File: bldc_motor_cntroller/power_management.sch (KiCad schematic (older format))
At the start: 29 parts, among them J8 XT60, J9 XT60, Q1 CSD18540Q5B, Q2 CSD18540Q5B, U2 TLV75733PDBV, U3 LM5109BSD

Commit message: added missing footprints.
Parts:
- R15, R18: footprint Capacitor_SMD:C_0402_1005Metric -> Resistor_SMD:R_0402_1005Metric
- R16, R17, R19: footprint (none) -> Resistor_SMD:R_0402_1005Metric
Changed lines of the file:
@@
 F 0 "R15" V 4900 5200 50  0000 C CNN
 F 1 "2R2" V 4800 5200 50  0000 C CNN
-F 2 "Capacitor_SMD:C_0402_1005Metric" V 4730 5200 50  0001 C CNN
+F 2 "Resistor_SMD:R_0402_1005Metric" V 4730 5200 50  0001 C CNN
 F 3 "~" H 4800 5200 50  0001 C CNN
 	1    4800 5200
@@
 F 0 "R18" V 4900 5950 50  0000 C CNN
 F 1 "2R2" V 4800 5950 50  0000 C CNN
-F 2 "Capacitor_SMD:C_0402_1005Metric" V 4730 5950 50  0001 C CNN
+F 2 "Resistor_SMD:R_0402_1005Metric" V 4730 5950 50  0001 C CNN
 F 3 "~" H 4800 5950 50  0001 C CNN
 	1    4800 5950
@@
 F 0 "R19" H 3280 6854 50  0000 R CNN
 F 1 "3.3k" H 3280 6945 50  0000 R CNN
-F 2 "" V 3280 6900 50  0001 C CNN
+F 2 "Resistor_SMD:R_0402_1005Metric" V 3280 6900 50  0001 C CNN
 F 3 "~" H 3350 6900 50  0001 C CNN
 	1    3350 6900
@@
 F 0 "R17" H 2430 5904 50  0000 R CNN
 F 1 "3.3k" H 2430 5995 50  0000 R CNN
-F 2 "" V 2430 5950 50  0001 C CNN
+F 2 "Resistor_SMD:R_0402_1005Metric" V 2430 5950 50  0001 C CNN
 F 3 "~" H 2500 5950 50  0001 C CNN
 	1    2500 5950
@@
 F 0 "R16" H 2080 5904 50  0000 R CNN
 F 1 "3.3k" H 2080 5995 50  0000 R CNN
-F 2 "" V 2080 5950 50  0001 C CNN
+F 2 "Resistor_SMD:R_0402_1005Metric" V 2080 5950 50  0001 C CNN
 F 3 "~" H 2150 5950 50  0001 C CNN
 	1    2150 5950

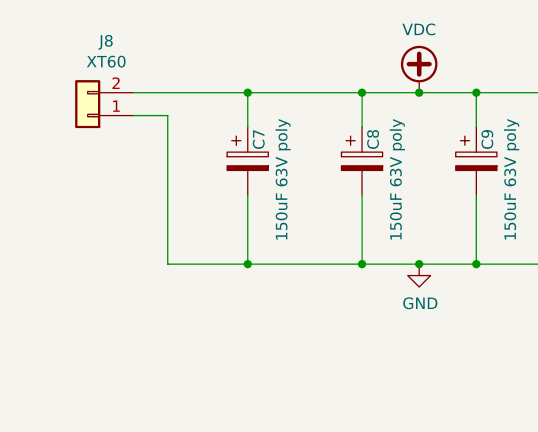
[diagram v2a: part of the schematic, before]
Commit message: pcb routing cont. swapped 2 motor output pins for better routing.
Signed-off-by: azmat bilal <azmat.bilal@outlook.com>
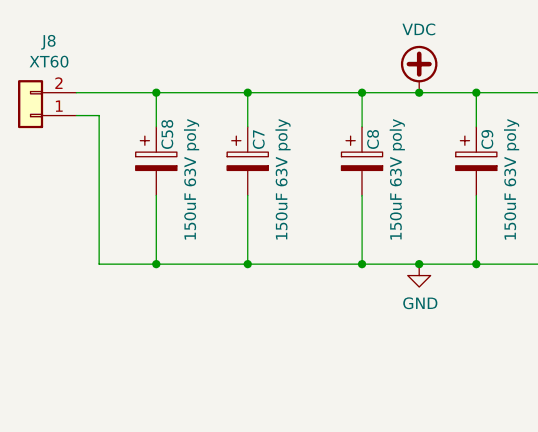
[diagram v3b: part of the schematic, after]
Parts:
- added C58: 150uF 63V poly, Capacitor_SMD:CP_Elec_10x14.3, symbol Device:CP
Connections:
- net GND: now also C58.2
- net VDC: now also C58.1
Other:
- moved on the sheet: J8
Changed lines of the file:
@@
 L Connector_Generic:Conn_01x02 J8
 U 1 1 5E3F134B
-P 1550 1750
-F 0 "J8" H 1468 1425 50  0000 C CNN
-F 1 "XT60" H 1468 1516 50  0000 C CNN
-F 2 "Connector_AMASS:AMASS_XT60-M_1x02_P7.20mm_Vertical" H 1550 1750 50  0001 C CNN
-F 3 "~" H 1550 1750 50  0001 C CNN
-	1    1550 1750
+P 1300 1750
+F 0 "J8" H 1218 1425 50  0000 C CNN
+F 1 "XT60" H 1218 1516 50  0000 C CNN
+F 2 "Connector_AMASS:AMASS_XT60-M_1x02_P7.20mm_Vertical" H 1300 1750 50  0001 C CNN
+F 3 "~" H 1300 1750 50  0001 C CNN
+	1    1300 1750
 	-1   0    0    1
 $EndComp
-Wire Wire Line
-	1750 1650 2250 1650
 Connection ~ 2250 1650
-Wire Wire Line
-	1750 1750 1900 1750
-Wire Wire Line
-	1900 1750 1900 2400
-Wire Wire Line
-	1900 2400 2250 2400
 Connection ~ 2250 2400
 $Comp
@@
 	0    1    1    0
 $EndComp
+$Comp
+L Device:CP C58
+U 1 1 5E4177F9
+P 1850 1950
+F 0 "C58" V 1900 2000 50  0000 L CNN
+F 1 "150uF 63V poly" V 2000 1600 50  0000 L CNN
+F 2 "Capacitor_SMD:CP_Elec_10x14.3" H 1888 1800 50  0001 C CNN
+F 3 "~" H 1850 1950 50  0001 C CNN
+F 4 "EEH-ZS1J151P" H 1850 1950 50  0001 C CNN "MPN"
+	1    1850 1950
+	1    0    0    -1
+$EndComp
+Wire Wire Line
+	1850 2100 1850 2400
+Wire Wire Line
+	1850 2400 2250 2400
+Wire Wire Line
+	1850 1800 1850 1650
+Connection ~ 1850 1650
+Wire Wire Line
+	1850 1650 2250 1650
+Wire Wire Line
+	1500 1650 1850 1650
+Wire Wire Line
+	1500 1750 1600 1750
+Wire Wire Line
+	1600 1750 1600 2400
+Wire Wire Line
+	1600 2400 1850 2400
+Connection ~ 1850 2400
 $EndSCHEMATC

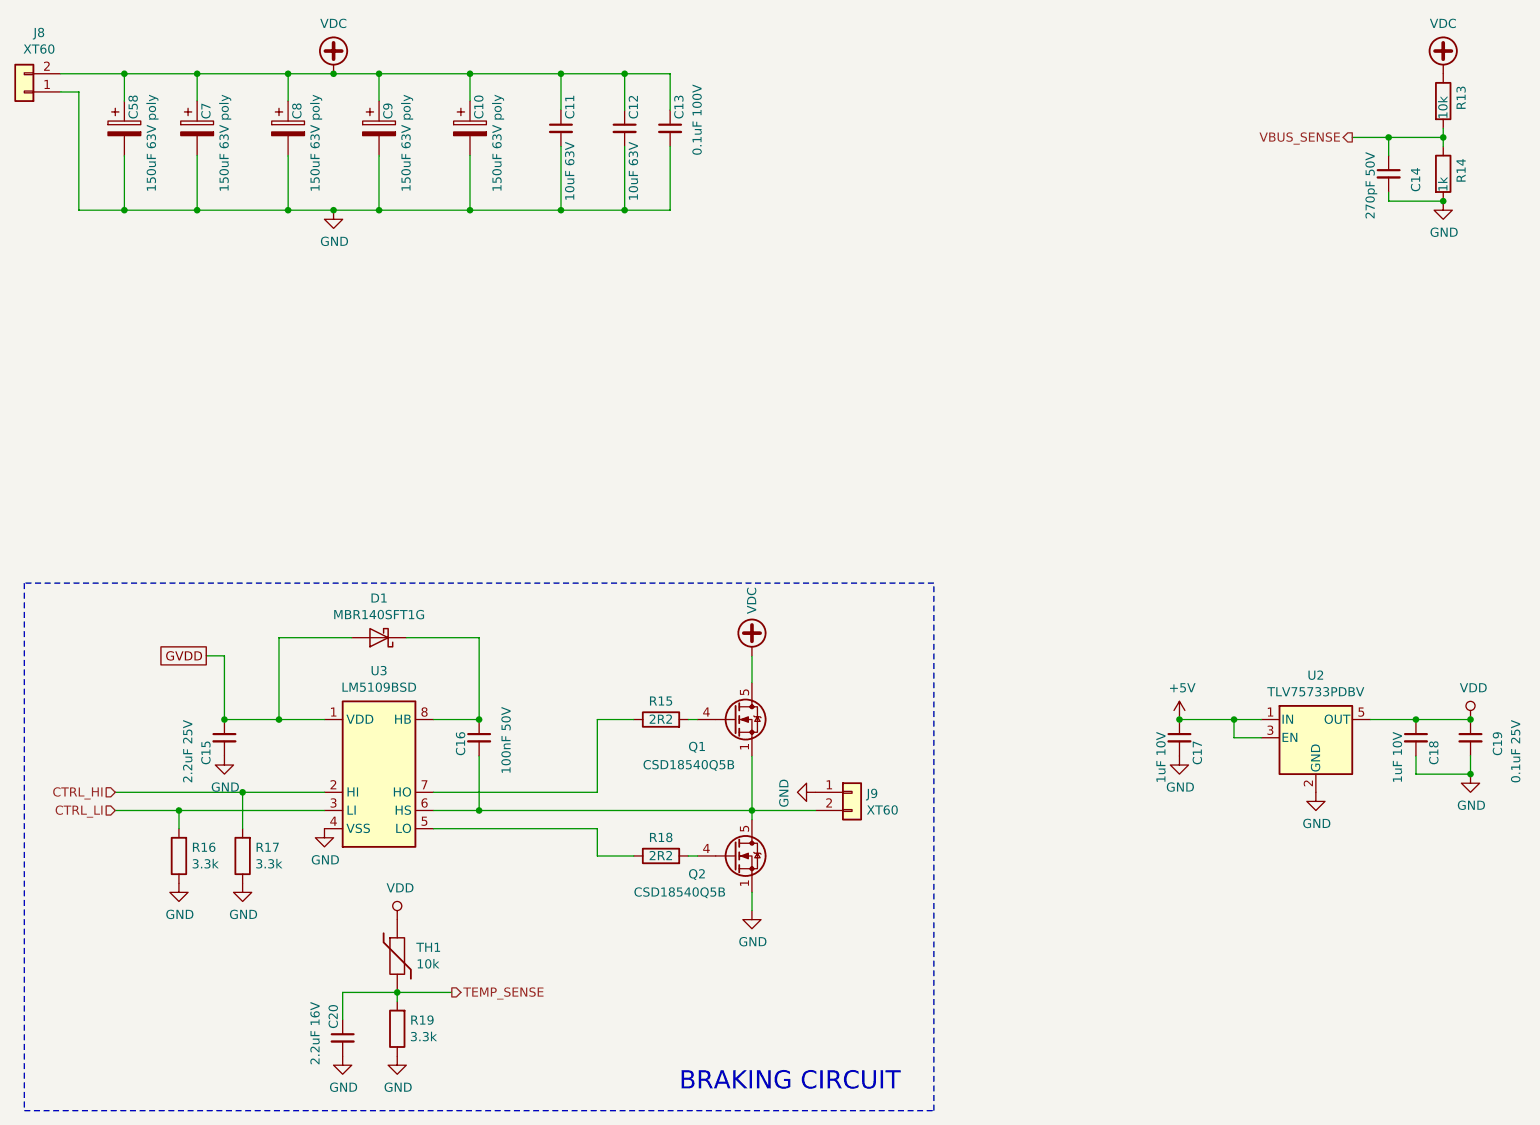
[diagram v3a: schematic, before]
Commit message: improved assembly documentation
Signed-off-by: azmat bilal <azmat.bilal@outlook.com>
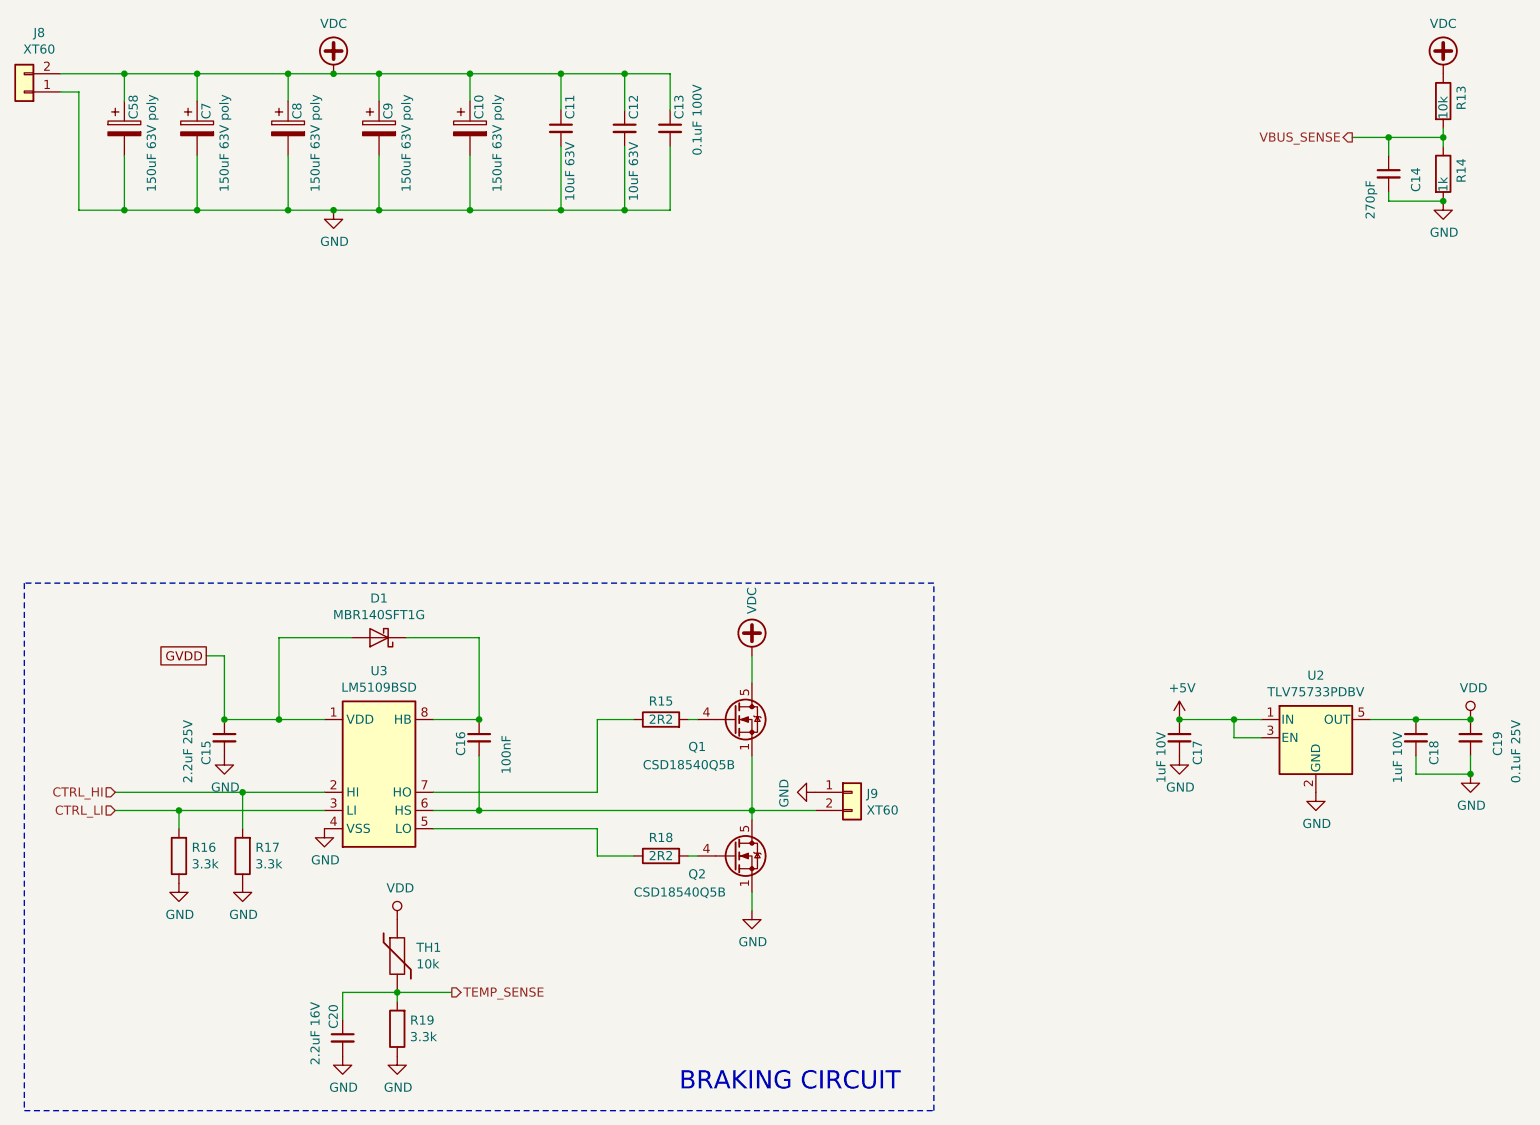
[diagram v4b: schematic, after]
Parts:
- C14: value 270pF 50V -> 270pF
- C16: value 100nF 50V -> 100nF
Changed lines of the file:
@@
 AR Path="/5E2D9349/5E4E3A84" Ref="C14"  Part="1"
 F 0 "C14" V 8950 2100 50  0000 L CNN
-F 1 "270pF 50V" V 8700 1950 50  0000 L CNN
+F 1 "270pF" V 8700 1950 50  0000 L CNN
 F 2 "Capacitor_SMD:C_0402_1005Metric" H 8800 2200 50  0001 C CNN
 F 3 "~" H 8800 2200 50  0001 C CNN
@@
 AR Path="/5E2D9349/5E366085" Ref="C16"  Part="1"
 F 0 "C16" V 3700 5200 50  0000 L CNN
-F 1 "100nF 50V" V 3950 5100 50  0000 L CNN
+F 1 "100nF" V 3950 5100 50  0000 L CNN
 F 2 "Capacitor_SMD:C_0402_1005Metric" H 3800 5300 50  0001 C CNN
 F 3 "~" H 3800 5300 50  0001 C CNN

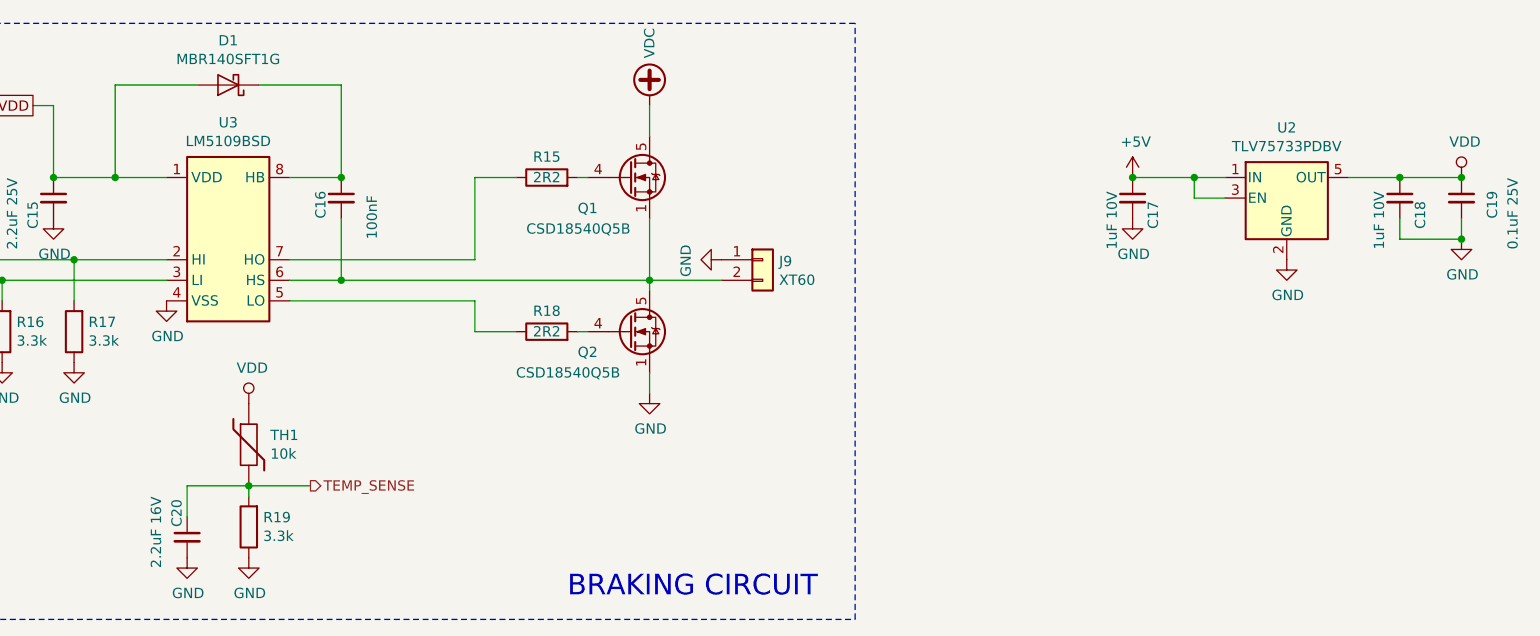
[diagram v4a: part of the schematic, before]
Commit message: improved BOM
Signed-off-by: azmat bilal <azmat.bilal@outlook.com>
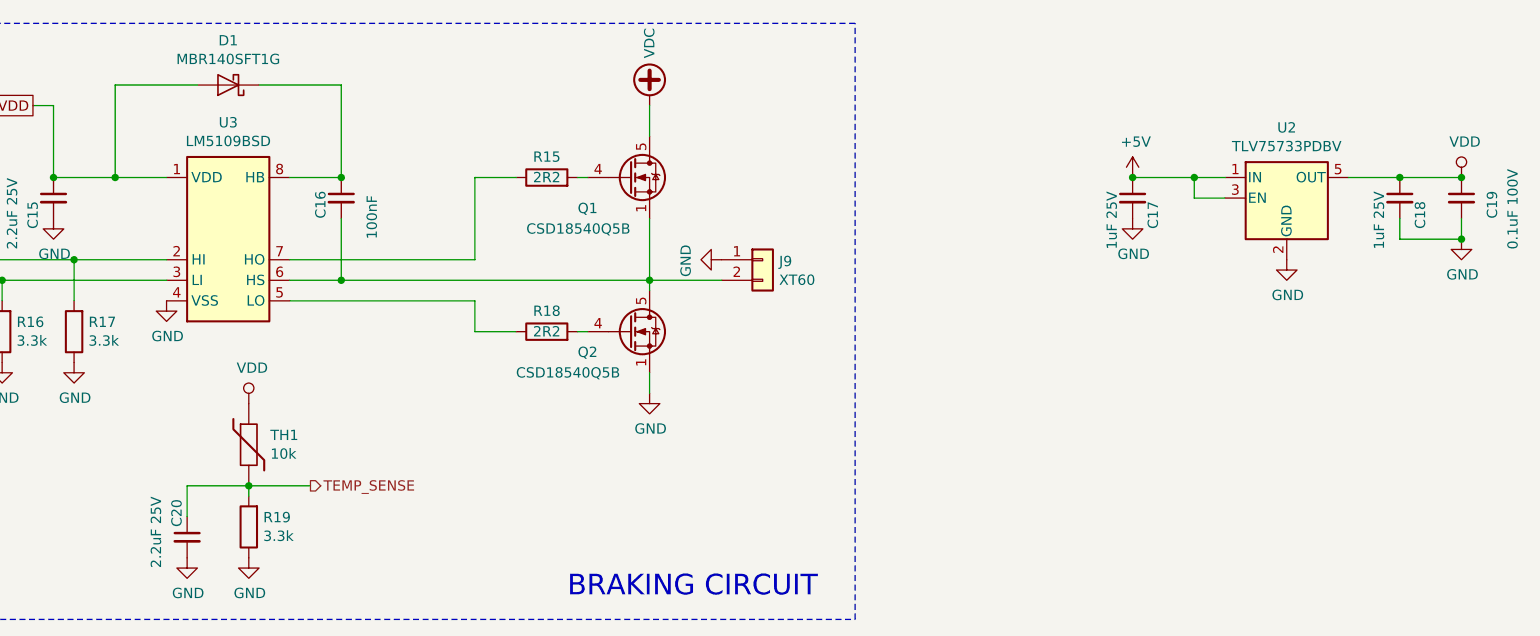
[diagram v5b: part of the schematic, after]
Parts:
- C13, C16: MPN (none) -> GRM155R62A104KE14D
- C14: MPN (none) -> GRM1555C1H271FA01D
- C15: MPN (none) -> GRM155C81E225KE11D
- C17, C18: value 1uF 10V -> 1uF 25V; MPN (none) -> GMK105CC6105MV-F
- C19: value 0.1uF 25V -> 0.1uF 100V; MPN (none) -> GRM155R62A104KE14D
- C20: value 2.2uF 16V -> 2.2uF 25V; MPN (none) -> GRM155C81E225KE11D
- D1: MPN (none) -> MBR140SFT1G
- J8, J9: MPN (none) -> XT60
- Q1, Q2: MPN (none) -> CSD18540Q5BT
- R13, TH1: MPN (none) -> CRCW040210K0FKEDC
- R14: MPN (none) -> ERJ-2RKF1001X
- R15, R18: MPN (none) -> CRCW04022R20FKEDC
- R16, R17, R19: MPN (none) -> CRCW04023K30FKEDC
- U2: MPN (none) -> TLV75733PDBV
- U3: MPN (none) -> LM5109BSDX/NOPB
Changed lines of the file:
@@
 F 2 "Resistor_SMD:R_0402_1005Metric" V 9030 1800 50  0001 C CNN
 F 3 "~" H 9100 1800 50  0001 C CNN
+F 4 "CRCW040210K0FKEDC" H 9100 1800 50  0001 C CNN "MPN"
 	1    9100 1800
 	1    0    0    -1
@@
 F 2 "Resistor_SMD:R_0402_1005Metric" V 9030 2200 50  0001 C CNN
 F 3 "~" H 9100 2200 50  0001 C CNN
+F 4 "ERJ-2RKF1001X" H 9100 2200 50  0001 C CNN "MPN"
 	1    9100 2200
 	1    0    0    -1
@@
 F 2 "Capacitor_SMD:C_0402_1005Metric" H 8800 2200 50  0001 C CNN
 F 3 "~" H 8800 2200 50  0001 C CNN
+F 4 "GRM1555C1H271FA01D" H 8800 2200 50  0001 C CNN "MPN"
 	1    8800 2200
 	1    0    0    -1
@@
 F 2 "Package_TO_SOT_SMD:SOT-23-5" H 8400 5625 50  0001 C CIN
 F 3 "https://www.ti.com/lit/ds/symlink/tlv757p.pdf" H 8400 5350 50  0001 C CNN
+F 4 "TLV75733PDBV" H 8400 5300 50  0001 C CNN "MPN"
 	1    8400 5300
 	1    0    0    -1
@@
 AR Path="/5E2D9349/5E3E815A" Ref="C18"  Part="1"
 F 0 "C18" V 9050 5150 50  0000 L CNN
-F 1 "1uF 10V" V 8850 5050 50  0000 L CNN
+F 1 "1uF 25V" V 8850 5050 50  0000 L CNN
 F 2 "Capacitor_SMD:C_0402_1005Metric" H 8950 5300 50  0001 C CNN
 F 3 "~" H 8950 5300 50  0001 C CNN
+F 4 "GMK105CC6105MV-F" H 8950 5300 50  0001 C CNN "MPN"
 	1    8950 5300
 	1    0    0    -1
@@
 AR Path="/5E2D9349/5E3E85BA" Ref="C19"  Part="1"
 F 0 "C19" V 9400 5200 50  0000 L CNN
-F 1 "0.1uF 25V" V 9500 5050 50  0000 L CNN
+F 1 "0.1uF 100V" V 9500 5050 50  0000 L CNN
 F 2 "Capacitor_SMD:C_0402_1005Metric" H 9250 5300 50  0001 C CNN
 F 3 "~" H 9250 5300 50  0001 C CNN
+F 4 "GRM155R62A104KE14D" H 9250 5300 50  0001 C CNN "MPN"
 	1    9250 5300
 	1    0    0    -1
@@
 AR Path="/5E2D9349/5E3E93E7" Ref="C17"  Part="1"
 F 0 "C17" V 7750 5150 50  0000 L CNN
-F 1 "1uF 10V" V 7550 5050 50  0000 L CNN
+F 1 "1uF 25V" V 7550 5050 50  0000 L CNN
 F 2 "Capacitor_SMD:C_0402_1005Metric" H 7650 5300 50  0001 C CNN
 F 3 "~" H 7650 5300 50  0001 C CNN
+F 4 "GMK105CC6105MV-F" H 7650 5300 50  0001 C CNN "MPN"
 	1    7650 5300
 	1    0    0    -1
@@
 F 2 "Capacitor_SMD:C_0402_1005Metric" H 4850 1950 50  0001 C CNN
 F 3 "~" H 4850 1950 50  0001 C CNN
+F 4 "GRM155R62A104KE14D" H 4850 1950 50  0001 C CNN "MPN"
 	1    4850 1950
 	1    0    0    -1
@@
 F 2 "Package_SON:WSON-8_4x4mm_P0.8mm" H 3250 4900 50  0001 C CIN
 F 3 "http://www.ti.com/lit/ds/symlink/lm5109b.pdf" H 3250 5500 50  0001 C CNN
+F 4 "LM5109BSDX/NOPB" H 3250 5500 50  0001 C CNN "MPN"
 	1    3250 5500
 	1    0    0    -1
@@
 F 2 "Package_TO_SOT_SMD:TDSON-8-1" H 5400 5125 50  0001 L CIN
 F 3 "http://www.ti.com/lit/gpn/csd18540q5b" V 5200 5200 50  0001 L CNN
+F 4 "CSD18540Q5BT" H 5200 5200 50  0001 C CNN "MPN"
 	1    5200 5200
 	1    0    0    -1
@@
 F 2 "Package_TO_SOT_SMD:TDSON-8-1" H 5400 5875 50  0001 L CIN
 F 3 "http://www.ti.com/lit/gpn/csd18540q5b" V 5200 5950 50  0001 L CNN
+F 4 "CSD18540Q5BT" H 5200 5950 50  0001 C CNN "MPN"
 	1    5200 5950
 	1    0    0    -1
@@
 F 2 "Resistor_SMD:R_0402_1005Metric" V 4730 5200 50  0001 C CNN
 F 3 "~" H 4800 5200 50  0001 C CNN
+F 4 "CRCW04022R20FKEDC" H 4800 5200 50  0001 C CNN "MPN"
 	1    4800 5200
 	0    -1   -1   0
@@
 F 2 "Resistor_SMD:R_0402_1005Metric" V 4730 5950 50  0001 C CNN
 F 3 "~" H 4800 5950 50  0001 C CNN
+F 4 "CRCW04022R20FKEDC" H 4800 5950 50  0001 C CNN "MPN"
 	1    4800 5950
 	0    -1   -1   0
@@
 F 3 "~" H 2400 5300 50  0001 C CNN
 F 4 "" H 2400 5300 50  0001 C CNN "Description"
+F 5 "GRM155C81E225KE11D" H 2400 5300 50  0001 C CNN "MPN"
 	1    2400 5300
 	1    0    0    -1
@@
 F 3 "~" H 3800 5300 50  0001 C CNN
 F 4 "" H 3800 5300 50  0001 C CNN "Description"
+F 5 "GRM155R62A104KE14D" H 3800 5300 50  0001 C CNN "MPN"
 	1    3800 5300
 	1    0    0    -1
@@
 F 2 "Diode_SMD:D_SOD-123F" H 3250 4750 50  0001 C CNN
 F 3 "~" H 3250 4750 50  0001 C CNN
+F 4 "MBR140SFT1G" H 3250 4750 50  0001 C CNN "MPN"
 	1    3250 4750
 	-1   0    0    1
@@
 F 2 "Resistor_SMD:R_0402_1005Metric" H 3350 6500 50  0001 C CNN
 F 3 "~" H 3350 6500 50  0001 C CNN
+F 4 "CRCW040210K0FKEDC" H 3350 6500 50  0001 C CNN "MPN"
 	1    3350 6500
 	1    0    0    -1
@@
 F 2 "Resistor_SMD:R_0402_1005Metric" V 3280 6900 50  0001 C CNN
 F 3 "~" H 3350 6900 50  0001 C CNN
+F 4 "CRCW04023K30FKEDC" H 3350 6900 50  0001 C CNN "MPN"
 	1    3350 6900
 	-1   0    0    1
@@
 AR Path="/5E2D9349/5E3660C6" Ref="C20"  Part="1"
 F 0 "C20" V 3000 7000 50  0000 L CNN
-F 1 "2.2uF 16V" V 2900 6800 50  0000 L CNN
+F 1 "2.2uF 25V" V 2900 6800 50  0000 L CNN
 F 2 "Capacitor_SMD:C_0402_1005Metric" H 3050 6950 50  0001 C CNN
 F 3 "~" H 3050 6950 50  0001 C CNN
+F 4 "GRM155C81E225KE11D" H 3050 6950 50  0001 C CNN "MPN"
 	1    3050 6950
 	1    0    0    -1
@@
 F 2 "Resistor_SMD:R_0402_1005Metric" V 2430 5950 50  0001 C CNN
 F 3 "~" H 2500 5950 50  0001 C CNN
+F 4 "CRCW04023K30FKEDC" H 2500 5950 50  0001 C CNN "MPN"
 	1    2500 5950
 	-1   0    0    1
@@
 F 2 "Resistor_SMD:R_0402_1005Metric" V 2080 5950 50  0001 C CNN
 F 3 "~" H 2150 5950 50  0001 C CNN
+F 4 "CRCW04023K30FKEDC" H 2150 5950 50  0001 C CNN "MPN"
 	1    2150 5950
 	-1   0    0    1
@@
 F 2 "Connector_AMASS:AMASS_XT60-M_1x02_P7.20mm_Vertical" H 1300 1750 50  0001 C CNN
 F 3 "~" H 1300 1750 50  0001 C CNN
+F 4 "XT60" H 1300 1750 50  0001 C CNN "MPN"
 	1    1300 1750
 	-1   0    0    1
@@
 F 2 "Connector_AMASS:AMASS_XT60-M_1x02_P7.20mm_Vertical" H 5850 5600 50  0001 C CNN
 F 3 "~" H 5850 5600 50  0001 C CNN
+F 4 "XT60" H 5850 5600 50  0001 C CNN "MPN"
 	1    5850 5600
 	1    0    0    -1
